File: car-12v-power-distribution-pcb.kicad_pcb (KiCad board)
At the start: 2 copper layers, 120 x 160 mm, 7 parts, among them J1 IN_BATT, J2 IN_ACC, J3 OUT_DASHCAM, J4 OUT_PHONE, J5 OUT_BOOST, J6 OUT_SPARE1, J7 OUT_SPARE2

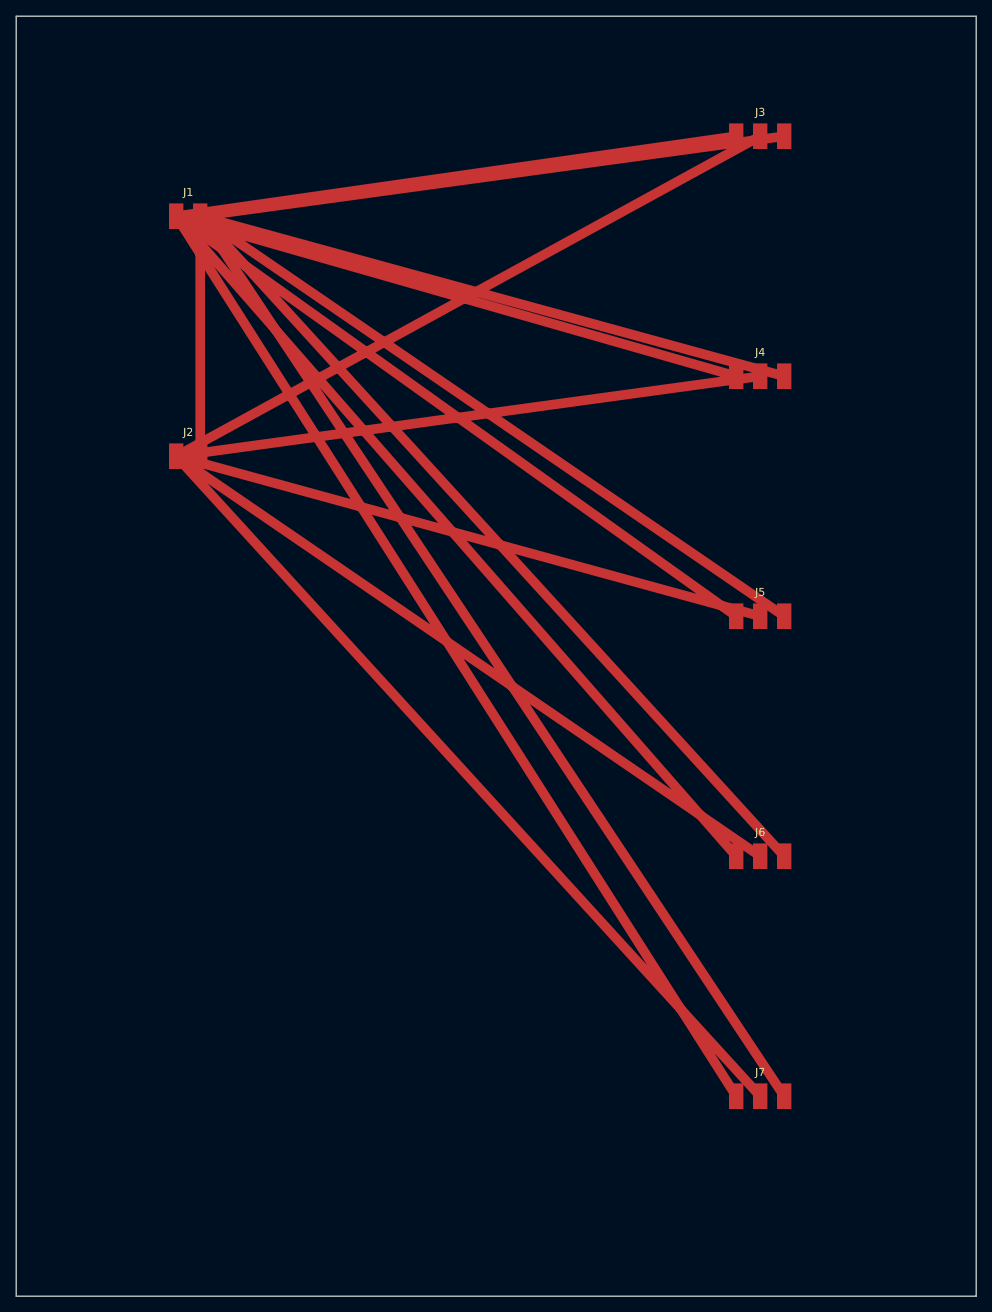
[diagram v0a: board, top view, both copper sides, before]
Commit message: Strip footprint properties for KiCad 6 PCB
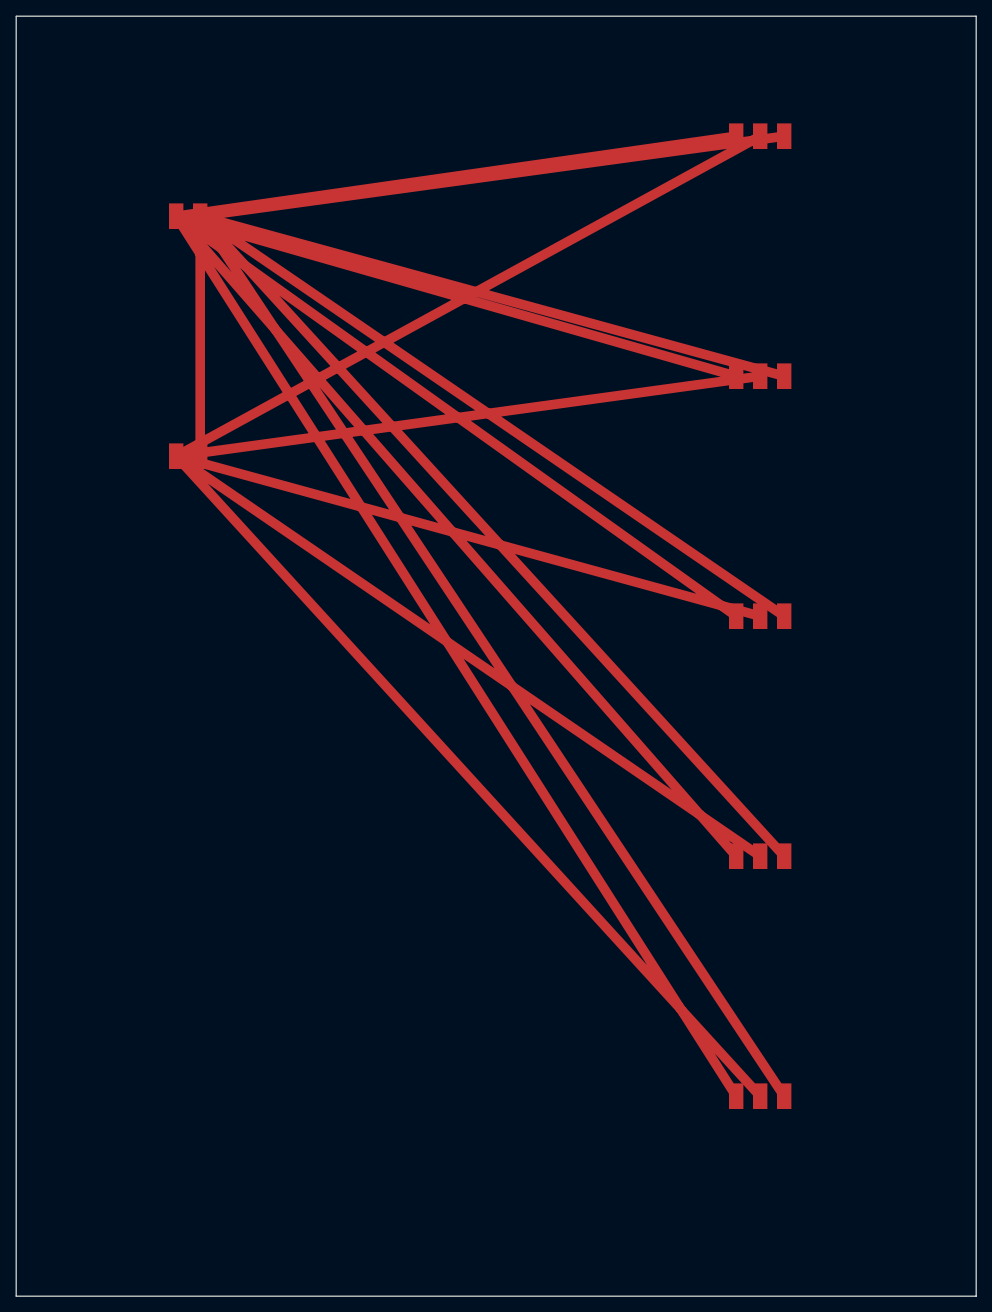
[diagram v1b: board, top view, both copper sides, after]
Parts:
- ?: renamed from J1; value IN_BATT -> (none)
- ?: renamed from J2; value IN_ACC -> (none)
- ?: renamed from J3; value OUT_DASHCAM -> (none)
- ?: renamed from J4; value OUT_PHONE -> (none)
- ?: renamed from J5; value OUT_BOOST -> (none)
- ?: renamed from J6; value OUT_SPARE1 -> (none)
- ?: renamed from J7; value OUT_SPARE2 -> (none)
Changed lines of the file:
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@@
   (footprint "PicoSpoX:PicoSpoX_1x02_P3.00mm_SMD" (layer "F.Cu")
     (at 40 40)
-    (property "Reference" "J1" (at 1.5 -3) (layer "F.SilkS") (effects (font (size 1 1) (thickness 0.15))))
-    (property "Value" "IN_BATT" (at 1.5 3) (layer "F.Fab") (effects (font (size 1 1) (thickness 0.15))))
     (pad "1" smd rect (at 0 0) (size 1.8 3.2) (layers "F.Cu" "F.Paste" "F.Mask") (net 2))
     (pad "2" smd rect (at 3 0) (size 1.8 3.2) (layers "F.Cu" "F.Paste" "F.Mask") (net 1))
@@
   (footprint "PicoSpoX:PicoSpoX_1x02_P3.00mm_SMD" (layer "F.Cu")
     (at 40 70)
-    (property "Reference" "J2" (at 1.5 -3) (layer "F.SilkS") (effects (font (size 1 1) (thickness 0.15))))
-    (property "Value" "IN_ACC" (at 1.5 3) (layer "F.Fab") (effects (font (size 1 1) (thickness 0.15))))
     (pad "1" smd rect (at 0 0) (size 1.8 3.2) (layers "F.Cu" "F.Paste" "F.Mask") (net 3))
     (pad "2" smd rect (at 3 0) (size 1.8 3.2) (layers "F.Cu" "F.Paste" "F.Mask") (net 1))
@@
   (footprint "PicoSpoX:PicoSpoX_1x03_P3.00mm_SMD" (layer "F.Cu")
     (at 110 30)
-    (property "Reference" "J3" (at 3 -3) (layer "F.SilkS") (effects (font (size 1 1) (thickness 0.15))))
-    (property "Value" "OUT_DASHCAM" (at 3 3) (layer "F.Fab") (effects (font (size 1 1) (thickness 0.15))))
     (pad "1" smd rect (at 0 0) (size 1.8 3.2) (layers "F.Cu" "F.Paste" "F.Mask") (net 2))
     (pad "2" smd rect (at 3 0) (size 1.8 3.2) (layers "F.Cu" "F.Paste" "F.Mask") (net 3))
@@
   (footprint "PicoSpoX:PicoSpoX_1x03_P3.00mm_SMD" (layer "F.Cu")
     (at 110 60)
-    (property "Reference" "J4" (at 3 -3) (layer "F.SilkS") (effects (font (size 1 1) (thickness 0.15))))
-    (property "Value" "OUT_PHONE" (at 3 3) (layer "F.Fab") (effects (font (size 1 1) (thickness 0.15))))
     (pad "1" smd rect (at 0 0) (size 1.8 3.2) (layers "F.Cu" "F.Paste" "F.Mask") (net 2))
     (pad "2" smd rect (at 3 0) (size 1.8 3.2) (layers "F.Cu" "F.Paste" "F.Mask") (net 3))
@@
   (footprint "PicoSpoX:PicoSpoX_1x03_P3.00mm_SMD" (layer "F.Cu")
     (at 110 90)
-    (property "Reference" "J5" (at 3 -3) (layer "F.SilkS") (effects (font (size 1 1) (thickness 0.15))))
-    (property "Value" "OUT_BOOST" (at 3 3) (layer "F.Fab") (effects (font (size 1 1) (thickness 0.15))))
     (pad "1" smd rect (at 0 0) (size 1.8 3.2) (layers "F.Cu" "F.Paste" "F.Mask") (net 2))
     (pad "2" smd rect (at 3 0) (size 1.8 3.2) (layers "F.Cu" "F.Paste" "F.Mask") (net 3))
@@
   (footprint "PicoSpoX:PicoSpoX_1x03_P3.00mm_SMD" (layer "F.Cu")
     (at 110 120)
-    (property "Reference" "J6" (at 3 -3) (layer "F.SilkS") (effects (font (size 1 1) (thickness 0.15))))
-    (property "Value" "OUT_SPARE1" (at 3 3) (layer "F.Fab") (effects (font (size 1 1) (thickness 0.15))))
     (pad "1" smd rect (at 0 0) (size 1.8 3.2) (layers "F.Cu" "F.Paste" "F.Mask") (net 2))
     (pad "2" smd rect (at 3 0) (size 1.8 3.2) (layers "F.Cu" "F.Paste" "F.Mask") (net 3))
@@
   (footprint "PicoSpoX:PicoSpoX_1x03_P3.00mm_SMD" (layer "F.Cu")
     (at 110 150)
-    (property "Reference" "J7" (at 3 -3) (layer "F.SilkS") (effects (font (size 1 1) (thickness 0.15))))
-    (property "Value" "OUT_SPARE2" (at 3 3) (layer "F.Fab") (effects (font (size 1 1) (thickness 0.15))))
     (pad "1" smd rect (at 0 0) (size 1.8 3.2) (layers "F.Cu" "F.Paste" "F.Mask") (net 2))
     (pad "2" smd rect (at 3 0) (size 1.8 3.2) (layers "F.Cu" "F.Paste" "F.Mask") (net 3))

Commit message: Reset to blank KiCad 6 schematic and PCB
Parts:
- removed ? (x2): , PicoSpoX:PicoSpoX_1x02_P3.00mm_SMD
- removed ? (x5): , PicoSpoX:PicoSpoX_1x03_P3.00mm_SMD
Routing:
- net GND: track 508.2 -> 0.00 mm
- net +12V_BATT: track 466.2 -> 0.00 mm
- net +12V_ACC: track 429.4 -> 0.00 mm
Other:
- board outline removed
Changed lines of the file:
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@@
       (layer "B.SilkS" (type "Bottom Silk Screen"))
-    )
-    (pcbplotparams
-      (layerselection 0x00010fc_ffffffff)
-      (plot_on_all_layers_selection 0x0000000_00000000)
-      (disableapertmacros false)
-      (usegerberextensions false)
-      (usegerberattributes true)
-      (usegerberadvancedattributes true)
-      (creategerberjobfile true)
-      (svguseinch false)
-      (svgprecision 6)
-      (excludeedgelayer true)
-      (plotframeref false)
-      (viasonmask false)
-      (mode 1)
-      (useauxorigin false)
-      (hpglpennumber 1)
-      (hpglpenspeed 20)
-      (hpglpendiameter 15)
-      (dxfpolygonmode true)
-      (dxfimperialunits true)
-      (dxfusepcbnewfont true)
-      (psnegative false)
-      (psa4output false)
-      (plotreference true)
-      (plotvalue true)
-      (plotinvisibletext false)
-      (sketchpadsonfab false)
-      (subtractmaskfromsilk false)
-      (outputformat 1)
-      (mirror false)
-      (drillshape 1)
-      (scaleselection 1)
-      (outputdirectory "")
     )
   )
   (net 0 "")
-  (net 1 "GND")
-  (net 2 "+12V_BATT")
-  (net 3 "+12V_ACC")
-  (footprint "PicoSpoX:PicoSpoX_1x02_P3.00mm_SMD" (layer "F.Cu")
-    (at 40 40)
-    (pad "1" smd rect (at 0 0) (size 1.8 3.2) (layers "F.Cu" "F.Paste" "F.Mask") (net 2))
-    (pad "2" smd rect (at 3 0) (size 1.8 3.2) (layers "F.Cu" "F.Paste" "F.Mask") (net 1))
-  )
-  (footprint "PicoSpoX:PicoSpoX_1x02_P3.00mm_SMD" (layer "F.Cu")
-    (at 40 70)
-    (pad "1" smd rect (at 0 0) (size 1.8 3.2) (layers "F.Cu" "F.Paste" "F.Mask") (net 3))
-    (pad "2" smd rect (at 3 0) (size 1.8 3.2) (layers "F.Cu" "F.Paste" "F.Mask") (net 1))
-  )
-  (footprint "PicoSpoX:PicoSpoX_1x03_P3.00mm_SMD" (layer "F.Cu")
-    (at 110 30)
-    (pad "1" smd rect (at 0 0) (size 1.8 3.2) (layers "F.Cu" "F.Paste" "F.Mask") (net 2))
-    (pad "2" smd rect (at 3 0) (size 1.8 3.2) (layers "F.Cu" "F.Paste" "F.Mask") (net 3))
-    (pad "3" smd rect (at 6 0) (size 1.8 3.2) (layers "F.Cu" "F.Paste" "F.Mask") (net 1))
-  )
-  (footprint "PicoSpoX:PicoSpoX_1x03_P3.00mm_SMD" (layer "F.Cu")
-    (at 110 60)
-    (pad "1" smd rect (at 0 0) (size 1.8 3.2) (layers "F.Cu" "F.Paste" "F.Mask") (net 2))
-    (pad "2" smd rect (at 3 0) (size 1.8 3.2) (layers "F.Cu" "F.Paste" "F.Mask") (net 3))
-    (pad "3" smd rect (at 6 0) (size 1.8 3.2) (layers "F.Cu" "F.Paste" "F.Mask") (net 1))
-  )
-  (footprint "PicoSpoX:PicoSpoX_1x03_P3.00mm_SMD" (layer "F.Cu")
-    (at 110 90)
-    (pad "1" smd rect (at 0 0) (size 1.8 3.2) (layers "F.Cu" "F.Paste" "F.Mask") (net 2))
-    (pad "2" smd rect (at 3 0) (size 1.8 3.2) (layers "F.Cu" "F.Paste" "F.Mask") (net 3))
-    (pad "3" smd rect (at 6 0) (size 1.8 3.2) (layers "F.Cu" "F.Paste" "F.Mask") (net 1))
-  )
-  (footprint "PicoSpoX:PicoSpoX_1x03_P3.00mm_SMD" (layer "F.Cu")
-    (at 110 120)
-    (pad "1" smd rect (at 0 0) (size 1.8 3.2) (layers "F.Cu" "F.Paste" "F.Mask") (net 2))
-    (pad "2" smd rect (at 3 0) (size 1.8 3.2) (layers "F.Cu" "F.Paste" "F.Mask") (net 3))
-    (pad "3" smd rect (at 6 0) (size 1.8 3.2) (layers "F.Cu" "F.Paste" "F.Mask") (net 1))
-  )
-  (footprint "PicoSpoX:PicoSpoX_1x03_P3.00mm_SMD" (layer "F.Cu")
-    (at 110 150)
-    (pad "1" smd rect (at 0 0) (size 1.8 3.2) (layers "F.Cu" "F.Paste" "F.Mask") (net 2))
-    (pad "2" smd rect (at 3 0) (size 1.8 3.2) (layers "F.Cu" "F.Paste" "F.Mask") (net 3))
-    (pad "3" smd rect (at 6 0) (size 1.8 3.2) (layers "F.Cu" "F.Paste" "F.Mask") (net 1))
-  )
-  (gr_rect (start 20 15) (end 140 175) (layer "Edge.Cuts") (width 0.05))
-  (segment (start 40 40) (end 110 30) (width 1.2) (layer "F.Cu") (net 2))
-  (segment (start 40 40) (end 110 60) (width 1.2) (layer "F.Cu") (net 2))
-  (segment (start 40 40) (end 110 90) (width 1.2) (layer "F.Cu") (net 2))
-  (segment (start 40 40) (end 110 120) (width 1.2) (layer "F.Cu") (net 2))
-  (segment (start 40 40) (end 110 150) (width 1.2) (layer "F.Cu") (net 2))
-  (segment (start 40 70) (end 113 30) (width 1.2) (layer "F.Cu") (net 3))
-  (segment (start 40 70) (end 113 60) (width 1.2) (layer "F.Cu") (net 3))
-  (segment (start 40 70) (end 113 90) (width 1.2) (layer "F.Cu") (net 3))
-  (segment (start 40 70) (end 113 120) (width 1.2) (layer "F.Cu") (net 3))
-  (segment (start 40 70) (end 113 150) (width 1.2) (layer "F.Cu") (net 3))
-  (segment (start 43 40) (end 43 70) (width 1.2) (layer "F.Cu") (net 1))
-  (segment (start 43 40) (end 116 30) (width 1.2) (layer "F.Cu") (net 1))
-  (segment (start 43 40) (end 116 60) (width 1.2) (layer "F.Cu") (net 1))
-  (segment (start 43 40) (end 116 90) (width 1.2) (layer "F.Cu") (net 1))
-  (segment (start 43 40) (end 116 120) (width 1.2) (layer "F.Cu") (net 1))
-  (segment (start 43 40) (end 116 150) (width 1.2) (layer "F.Cu") (net 1))
 )

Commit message: version 1.0
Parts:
- added D1: LED, LED_SMD:LED_0805_2012Metric, F.Cu at (74.8, 68.6)
- added D2: LED, LED_SMD:LED_0805_2012Metric, F.Cu at (74.8, 65.8)
- added D3: LED, LED_SMD:LED_0805_2012Metric, F.Cu at (74.8, 63.0)
- added H1: MountingHole, MountingHole:MountingHole_2.7mm_M2.5, F.Cu at (50.8, 38.1)
- added H2: MountingHole, MountingHole:MountingHole_2.7mm_M2.5, F.Cu at (91.4, 38.1)
- added H3: MountingHole, MountingHole:MountingHole_2.7mm_M2.5, F.Cu at (91.4, 66.0)
- added H4: MountingHole, MountingHole:MountingHole_2.7mm_M2.5, F.Cu at (50.8, 66.0)
- added J1: Conn_01x04, molex-picospox-0874370231_01x04:CONN_874370231-SD_04_MOL, F.Cu at (58.1, 40.6)
- added J2: Conn_01x03, molex-picospox-0874370231_01x03:CONN_874370231-SD_03_MOL, F.Cu at (71.1, 41.7)
- added J3: Conn_01x04, molex-picospox-0874370231_01x04:CONN_874370231-SD_04_MOL, F.Cu at (58.1, 50.8)
- added J4: Conn_01x04, molex-picospox-0874370231_01x04:CONN_874370231-SD_04_MOL, F.Cu at (58.1, 61.0)
- added J5: Conn_01x03, molex-picospox-0874370231_01x03:CONN_874370231-SD_03_MOL, F.Cu at (71.1, 51.8)
- added J6: Conn_01x03, molex-picospox-0874370231_01x03:CONN_874370231-SD_03_MOL, F.Cu at (83.3, 41.7)
- added J7: Conn_01x03, molex-picospox-0874370231_01x03:CONN_874370231-SD_03_MOL, F.Cu at (83.3, 51.8)
- added R1: 500, Resistor_SMD:R_0603_1608Metric, F.Cu at (78.6, 68.6)
- added R2: 500, Resistor_SMD:R_0603_1608Metric, F.Cu at (78.6, 65.8)
- added R3: 500, Resistor_SMD:R_0603_1608Metric, F.Cu at (78.6, 63.0)
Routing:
- net +12V: track 0.00 -> 111.7 mm
- net 12V_ACC: track 0.00 -> 104.5 mm
- net 12V_HEADLIGHT: track 0.00 -> 48.5 mm
- net Net-(D3-Pad1): track 0.00 -> 2.05 mm
- net Net-(D2-Pad1): track 0.00 -> 2.05 mm
- net Net-(D1-Pad1): track 0.00 -> 2.05 mm
- net GND: vias 0 -> 27
- added copper zone on B.Cu, net GND
- added copper zone on F.Cu, net GND
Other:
- board outline added: 50.8 x 38.1 mm
- board text added: "+"
- board text added: "12V+"
- board text added: "12V_ACC"
- board text added: "ACC POWER PCB V1.0 SMOOSE 02-28-26"
- board text added: "AIR TEMP"
- board text added: "BOOST"
- board text added: "CHARGER"
- board text added: "DASHCAM"
- board text added: "HLIGHT"
- board text added: "INPUT"

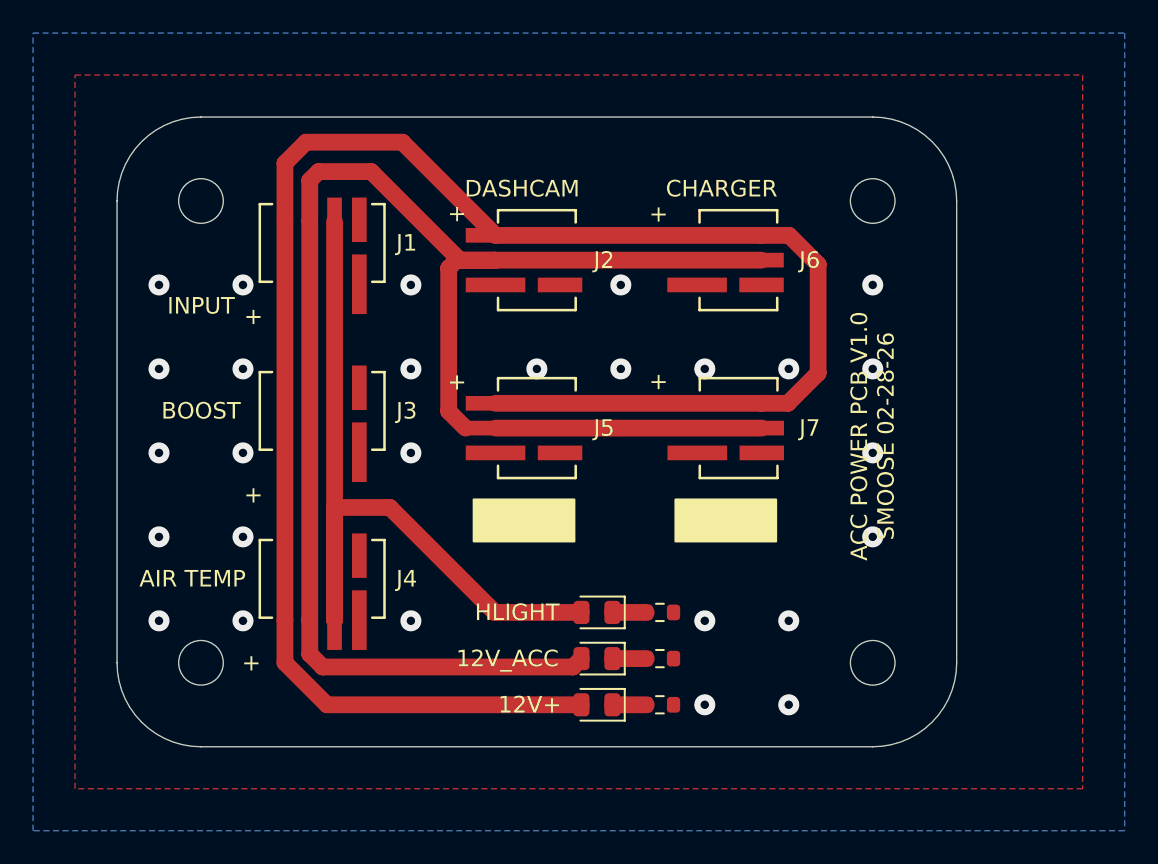
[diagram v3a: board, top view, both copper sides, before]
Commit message: updated grounding hole
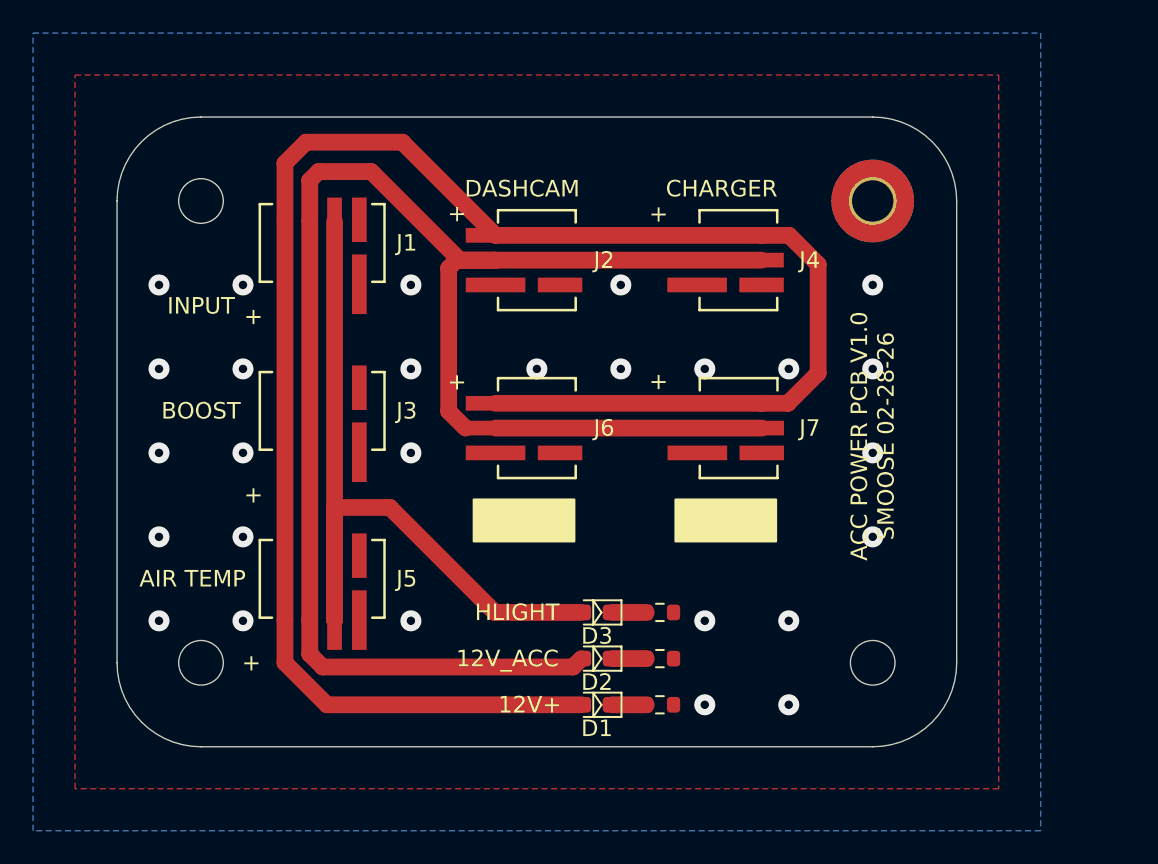
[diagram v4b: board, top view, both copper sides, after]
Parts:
- D1, D2, D3: footprint LED_SMD:LED_0805_2012Metric -> LED_SMD:LED_0603_1608Metric
- H2: value MountingHole -> MountingHole_Pad; footprint MountingHole:MountingHole_2.7mm_M2.5 -> MountingHole:MountingHole_2.5mm_Pad_TopBottom
- renumbered J6 to J4, J4 to J5, J5 to J6
